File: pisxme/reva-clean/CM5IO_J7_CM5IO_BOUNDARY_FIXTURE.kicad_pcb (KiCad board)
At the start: 6 copper layers, 98 x 110 mm, 7 parts, among them J2 A70-112-331N126, J7 Raspberry-Pi-5-Compute-Module, J7_BOUNDARY J7_LAUNCH_BOUNDARY, J9 THD-02-R, U6 TPD4EUSB30, U9 TPD4EUSB30

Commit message: phase17: record outer bridge trial
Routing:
- net CM5_GBE_TD1_P: track 200.6 -> 249.6 mm, vias 2 -> 3
- net CM5_GBE_TD1_N: track 209.8 -> 256.1 mm, vias 2 -> 3
- net CM5_GBE_TD3_P: track 84.6 -> 125.6 mm, vias 1 -> 2
- net CM5_GBE_TD0_N: track 210.8 -> 251.4 mm
- net CM5_GBE_TD3_N: track 89.3 -> 127.5 mm, vias 1 -> 2
- net CM5_GBE_TD0_P: track 204.3 -> 239.8 mm
- net CM5_GBE_TD2_N: track 94.8 -> 127.4 mm, vias 1 -> 2
- net CM5_GBE_TD2_P: track 98.0 -> 129.4 mm, vias 1 -> 2
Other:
- board size 98 x 110 mm -> 95 x 75 mm

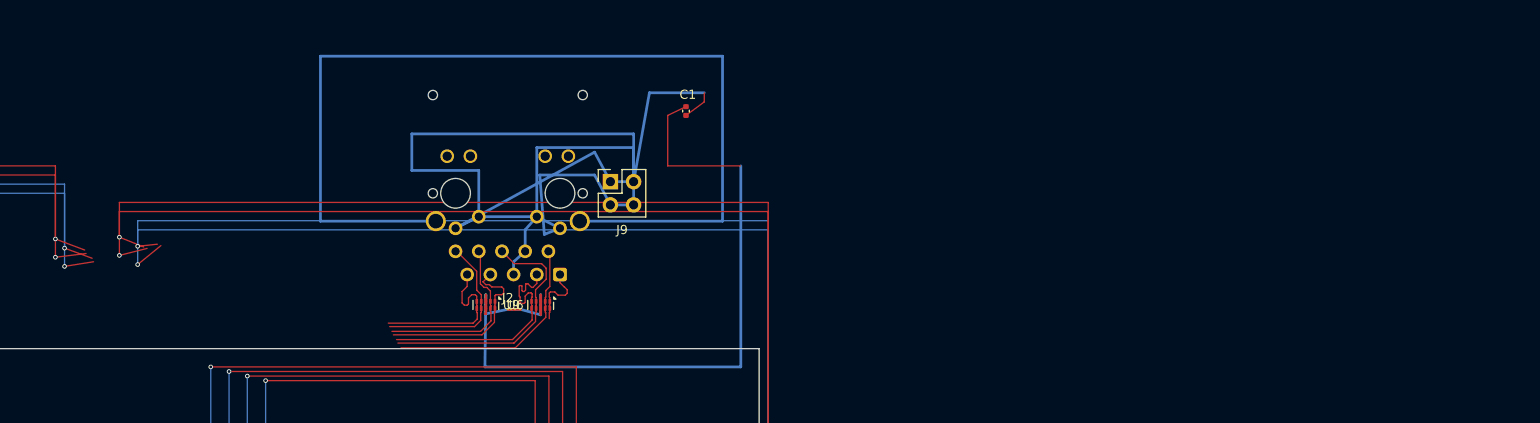
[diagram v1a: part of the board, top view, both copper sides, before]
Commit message: phase17: test remote ethernet island placement
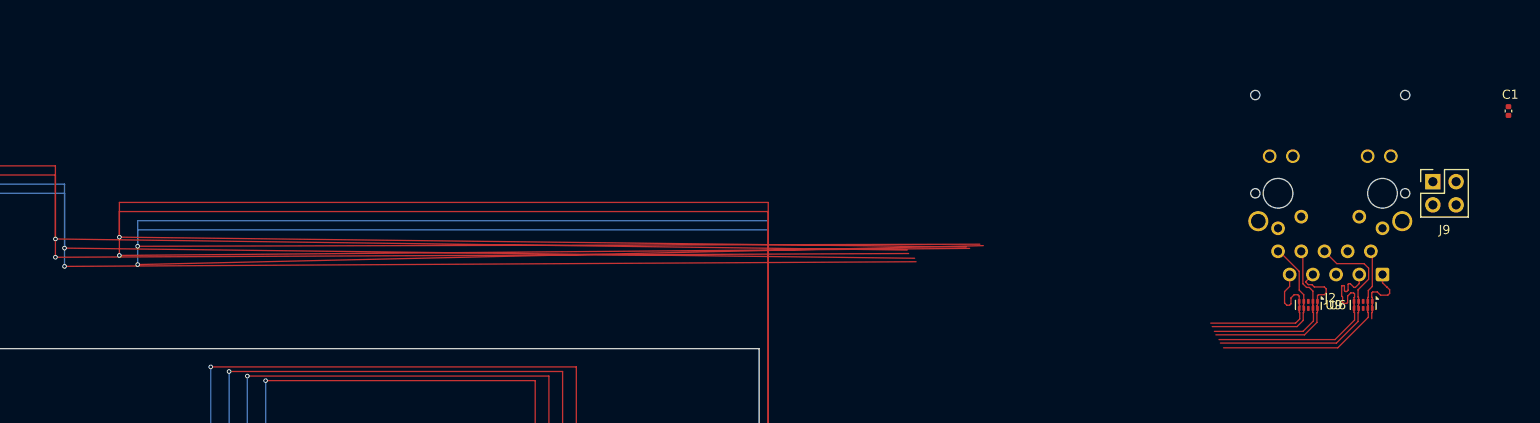
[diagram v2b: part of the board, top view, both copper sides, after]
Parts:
- moved C1 90.0 mm to (182.0, 44.0)
- moved J2 90.0 mm to (162.5, 53.0)
- moved U6 90.0 mm to (166.1, 65.2)
- moved U9 90.0 mm to (160.1, 65.2)
- moved J9 90.0 mm to (173.7, 51.7)
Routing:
- net ETH_CT_COMMON: track 153.2 -> 0.00 mm
- net GBE_SHIELD: track 108.3 -> 0.00 mm
- net CM5_GBE_TD0_N: track 251.4 -> 341.3 mm
- net CM5_GBE_TD3_N: track 127.5 -> 217.5 mm
- net CM5_GBE_TD2_P: track 129.4 -> 219.3 mm
- net CM5_GBE_TD1_N: track 256.1 -> 346.0 mm
- net ETH_GND: track 89.9 -> 0.00 mm
- net CM5_GBE_TD2_N: track 127.4 -> 217.2 mm
- net CM5_GBE_TD1_P: track 249.6 -> 339.4 mm
- net CM5_GBE_TD3_P: track 125.6 -> 215.4 mm
- net CM5_GBE_TD0_P: track 239.8 -> 329.0 mm

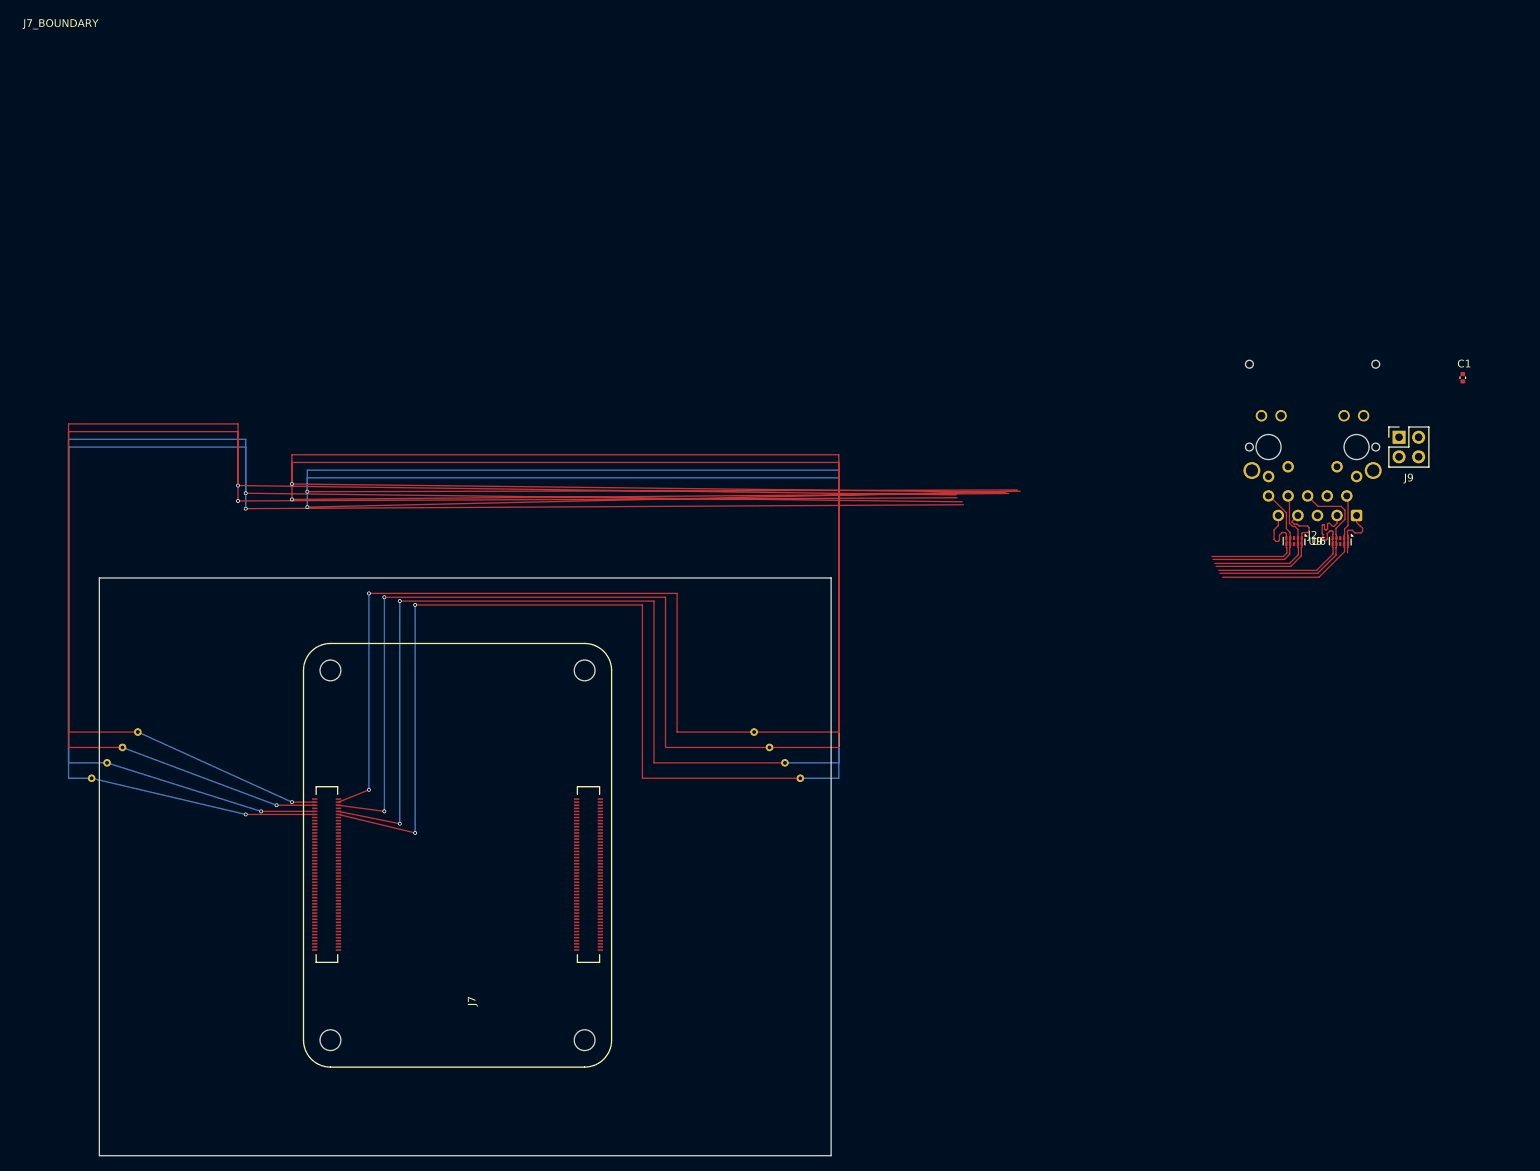
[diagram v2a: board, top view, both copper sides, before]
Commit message: phase17: publish round bridge blocker
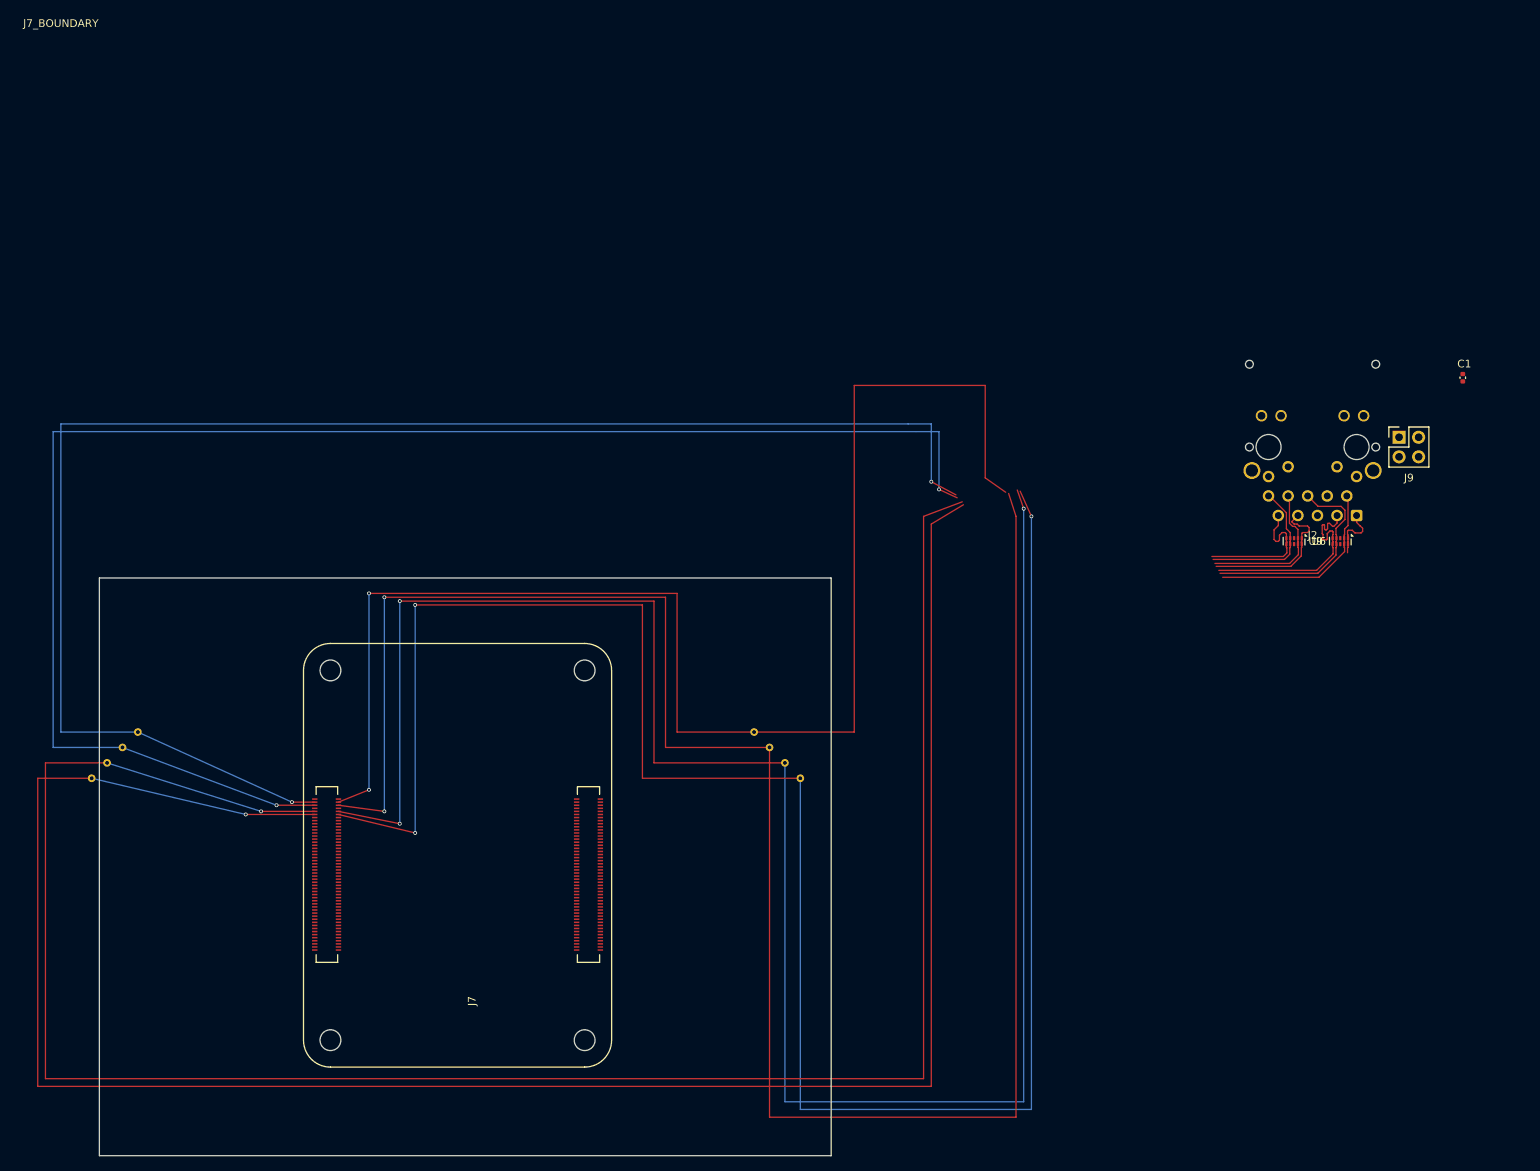
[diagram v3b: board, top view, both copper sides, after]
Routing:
- net CM5_GBE_TD1_P: track 339.4 -> 215.2 mm, vias 3 -> 2
- net CM5_GBE_TD2_N: track 217.2 -> 288.5 mm, vias 2 -> 1
- net CM5_GBE_TD2_P: track 219.3 -> 290.0 mm, vias 2 -> 1
- net CM5_GBE_TD0_P: track 329.0 -> 273.3 mm
- net CM5_GBE_TD0_N: track 341.3 -> 286.9 mm
- net CM5_GBE_TD1_N: track 346.0 -> 292.3 mm, vias 3 -> 2
- net CM5_GBE_TD3_N: track 217.5 -> 220.2 mm
- net CM5_GBE_TD3_P: track 215.4 -> 217.3 mm

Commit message: phase17: test ethernet pair permutation
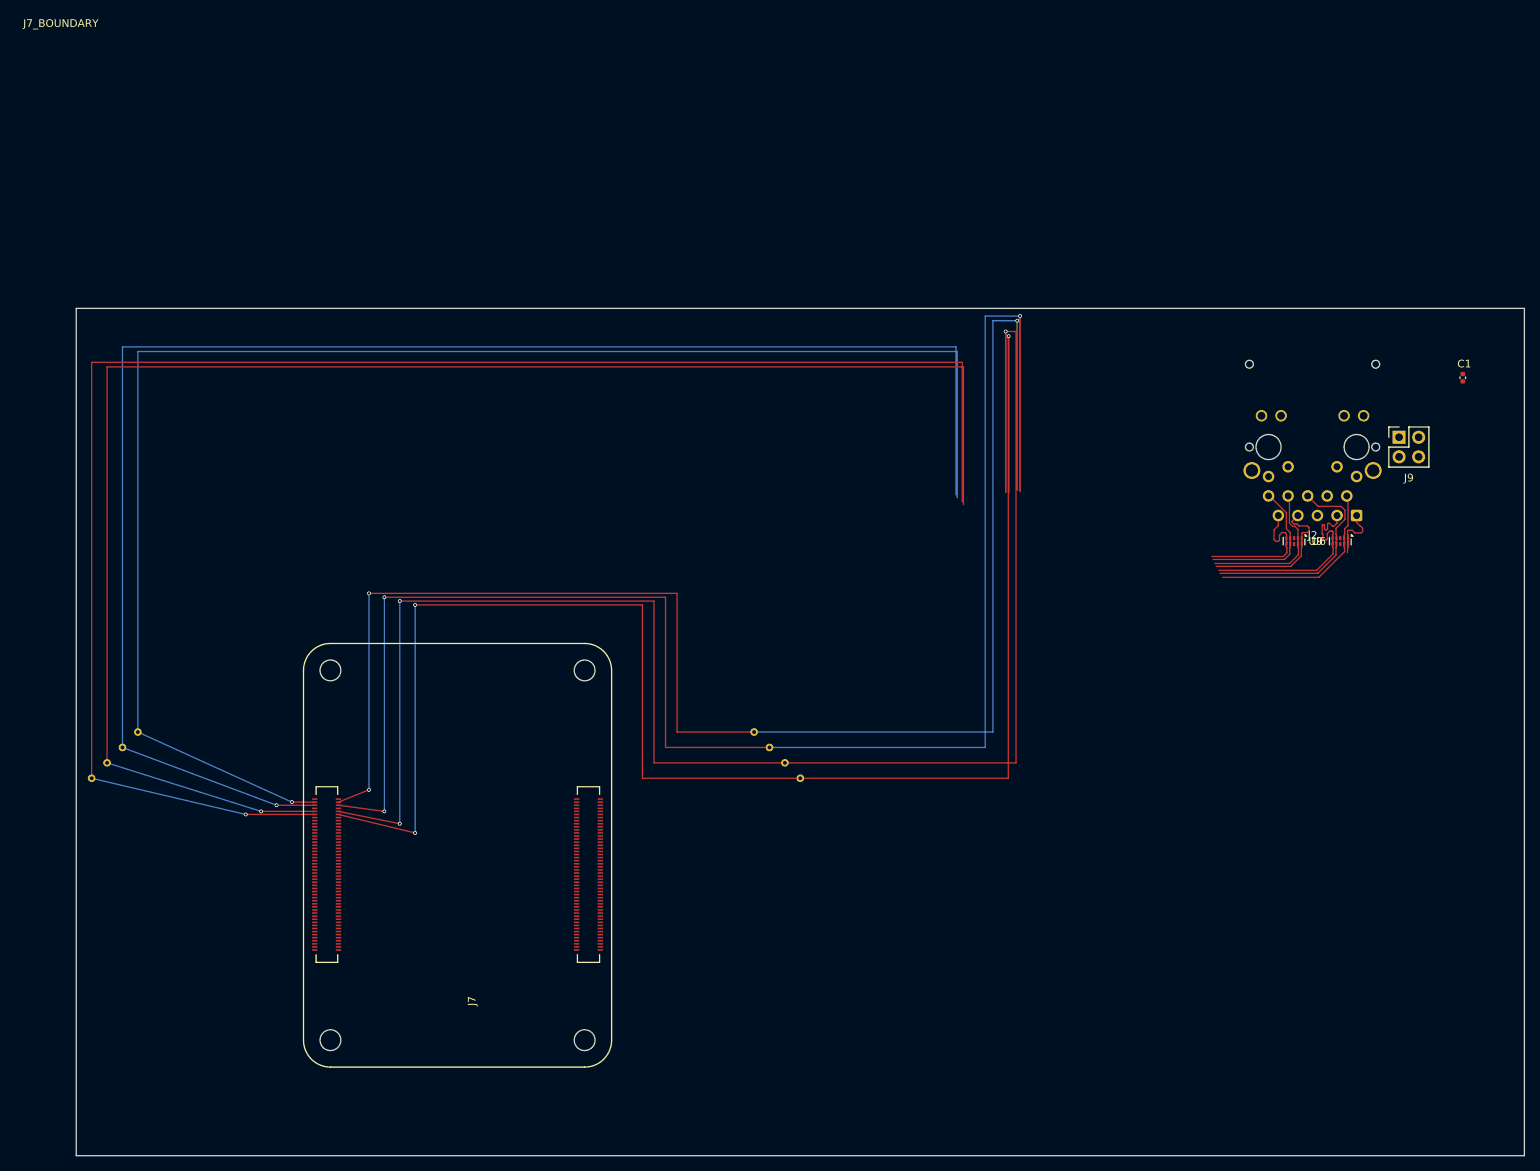
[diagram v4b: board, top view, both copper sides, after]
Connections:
- J2 pad 1: CM5_GBE_TD0_P -> CM5_GBE_TD1_N
- J2 pad 10: CM5_GBE_TD3_N -> CM5_GBE_TD3_P
- J2 pad 2: CM5_GBE_TD0_N -> CM5_GBE_TD1_P
- J2 pad 3: CM5_GBE_TD1_P -> CM5_GBE_TD0_N
- J2 pad 6: CM5_GBE_TD1_N -> CM5_GBE_TD0_P
- J2 pad 7: CM5_GBE_TD2_P -> CM5_GBE_TD2_N
- J2 pad 8: CM5_GBE_TD2_N -> CM5_GBE_TD2_P
- J2 pad 9: CM5_GBE_TD3_P -> CM5_GBE_TD3_N
- U6 pad 1: CM5_GBE_TD0_P -> CM5_GBE_TD1_N
- U6 pad 10: CM5_GBE_TD0_P -> CM5_GBE_TD1_N
- U6 pad 2: CM5_GBE_TD0_N -> CM5_GBE_TD1_P
- U6 pad 4: CM5_GBE_TD1_N -> CM5_GBE_TD0_P
- U6 pad 5: CM5_GBE_TD1_P -> CM5_GBE_TD0_N
- U6 pad 6: CM5_GBE_TD1_P -> CM5_GBE_TD0_N
- U6 pad 7: CM5_GBE_TD1_N -> CM5_GBE_TD0_P
- U6 pad 9: CM5_GBE_TD0_N -> CM5_GBE_TD1_P
- U9 pad 1: CM5_GBE_TD2_P -> CM5_GBE_TD2_N
- U9 pad 10: CM5_GBE_TD2_P -> CM5_GBE_TD2_N
- U9 pad 2: CM5_GBE_TD2_N -> CM5_GBE_TD2_P
- U9 pad 4: CM5_GBE_TD3_N -> CM5_GBE_TD3_P
- U9 pad 5: CM5_GBE_TD3_P -> CM5_GBE_TD3_N
- U9 pad 6: CM5_GBE_TD3_P -> CM5_GBE_TD3_N
- U9 pad 7: CM5_GBE_TD3_N -> CM5_GBE_TD3_P
- U9 pad 9: CM5_GBE_TD2_N -> CM5_GBE_TD2_P
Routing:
- net CM5_GBE_TD2_N: track 288.5 -> 228.0 mm
- net CM5_GBE_TD2_P: track 290.0 -> 233.9 mm
- net CM5_GBE_TD1_N: track 292.3 -> 244.6 mm, vias 2 -> 3
- net CM5_GBE_TD1_P: track 215.2 -> 253.6 mm, vias 2 -> 3
- net CM5_GBE_TD0_N: track 286.9 -> 264.3 mm
- net CM5_GBE_TD0_P: track 273.3 -> 265.5 mm
- net CM5_GBE_TD3_N: track 220.2 -> 224.0 mm, vias 2 -> 1
- net CM5_GBE_TD3_P: track 217.3 -> 218.5 mm, vias 2 -> 1
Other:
- board size 95 x 75 mm -> 188 x 110 mm

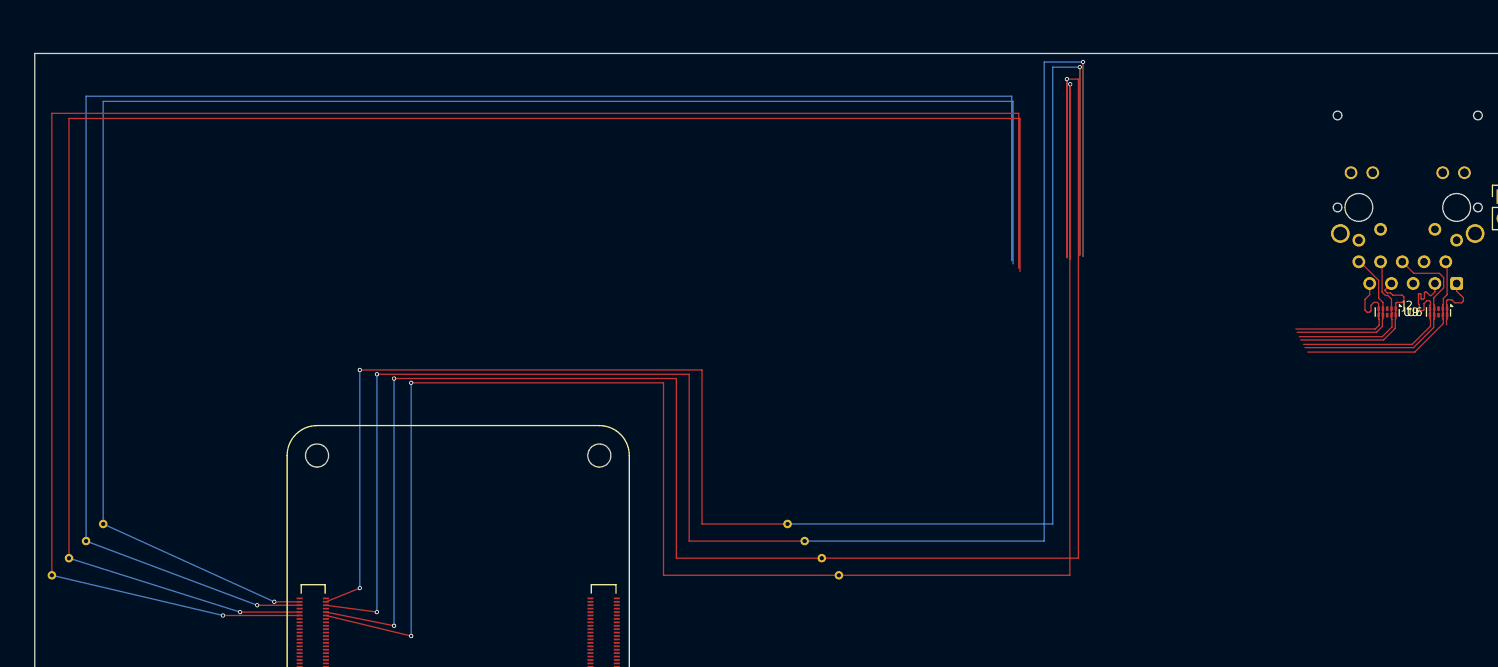
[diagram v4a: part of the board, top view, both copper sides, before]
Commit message: phase17: correct ethernet handoff endpoints
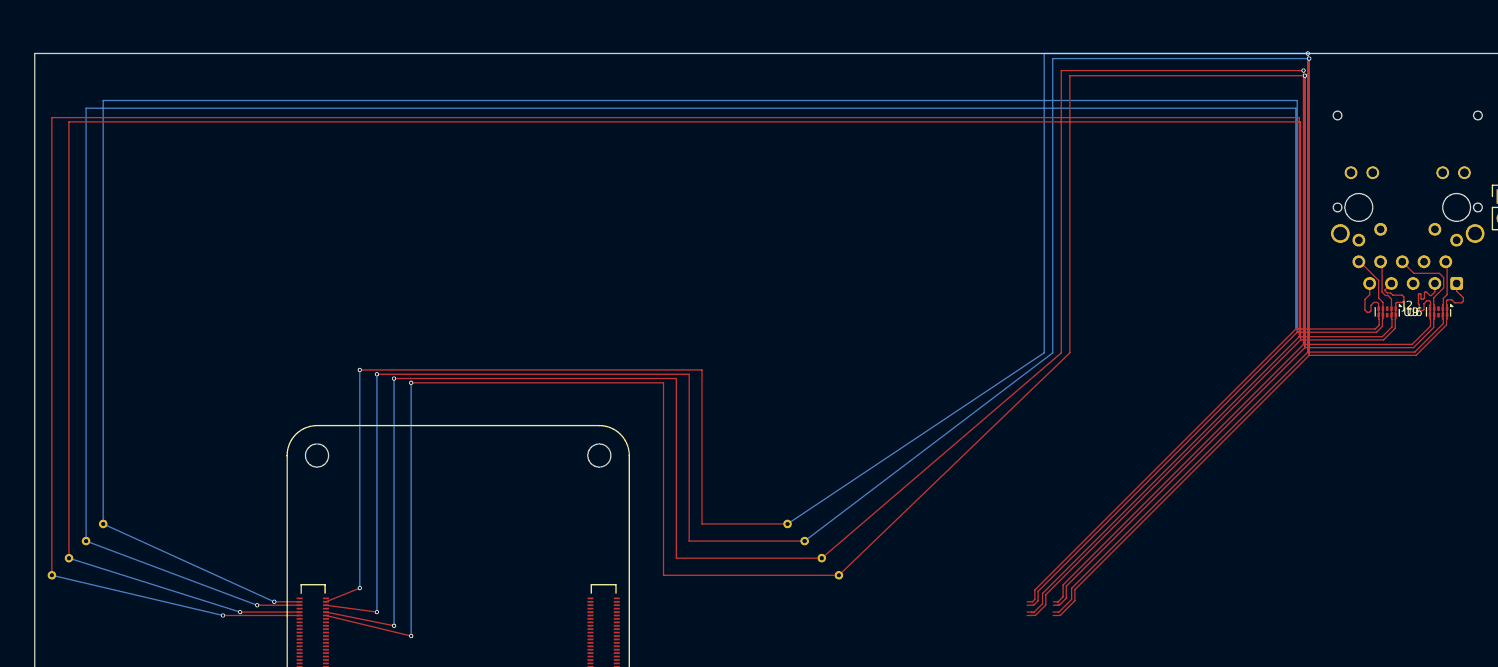
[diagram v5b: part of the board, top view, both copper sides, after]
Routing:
- net CM5_GBE_TD1_N: track 244.6 -> 341.6 mm
- net CM5_GBE_TD3_P: track 218.5 -> 305.3 mm
- net CM5_GBE_TD2_N: track 228.0 -> 314.1 mm
- net CM5_GBE_TD2_P: track 233.9 -> 319.6 mm
- net CM5_GBE_TD3_N: track 224.0 -> 307.7 mm
- net CM5_GBE_TD1_P: track 253.6 -> 337.0 mm
- net CM5_GBE_TD0_P: track 265.5 -> 343.8 mm
- net CM5_GBE_TD0_N: track 264.3 -> 339.9 mm
